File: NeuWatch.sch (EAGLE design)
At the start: 60 parts, among them IC1 SAMD21G18A-AUT, IC3 TPS2115, IC4 SIP32401A, IC5 MC74VHC1G14DFT, T1 846, T2 2N7002_ALT, Y1 32,768Khz

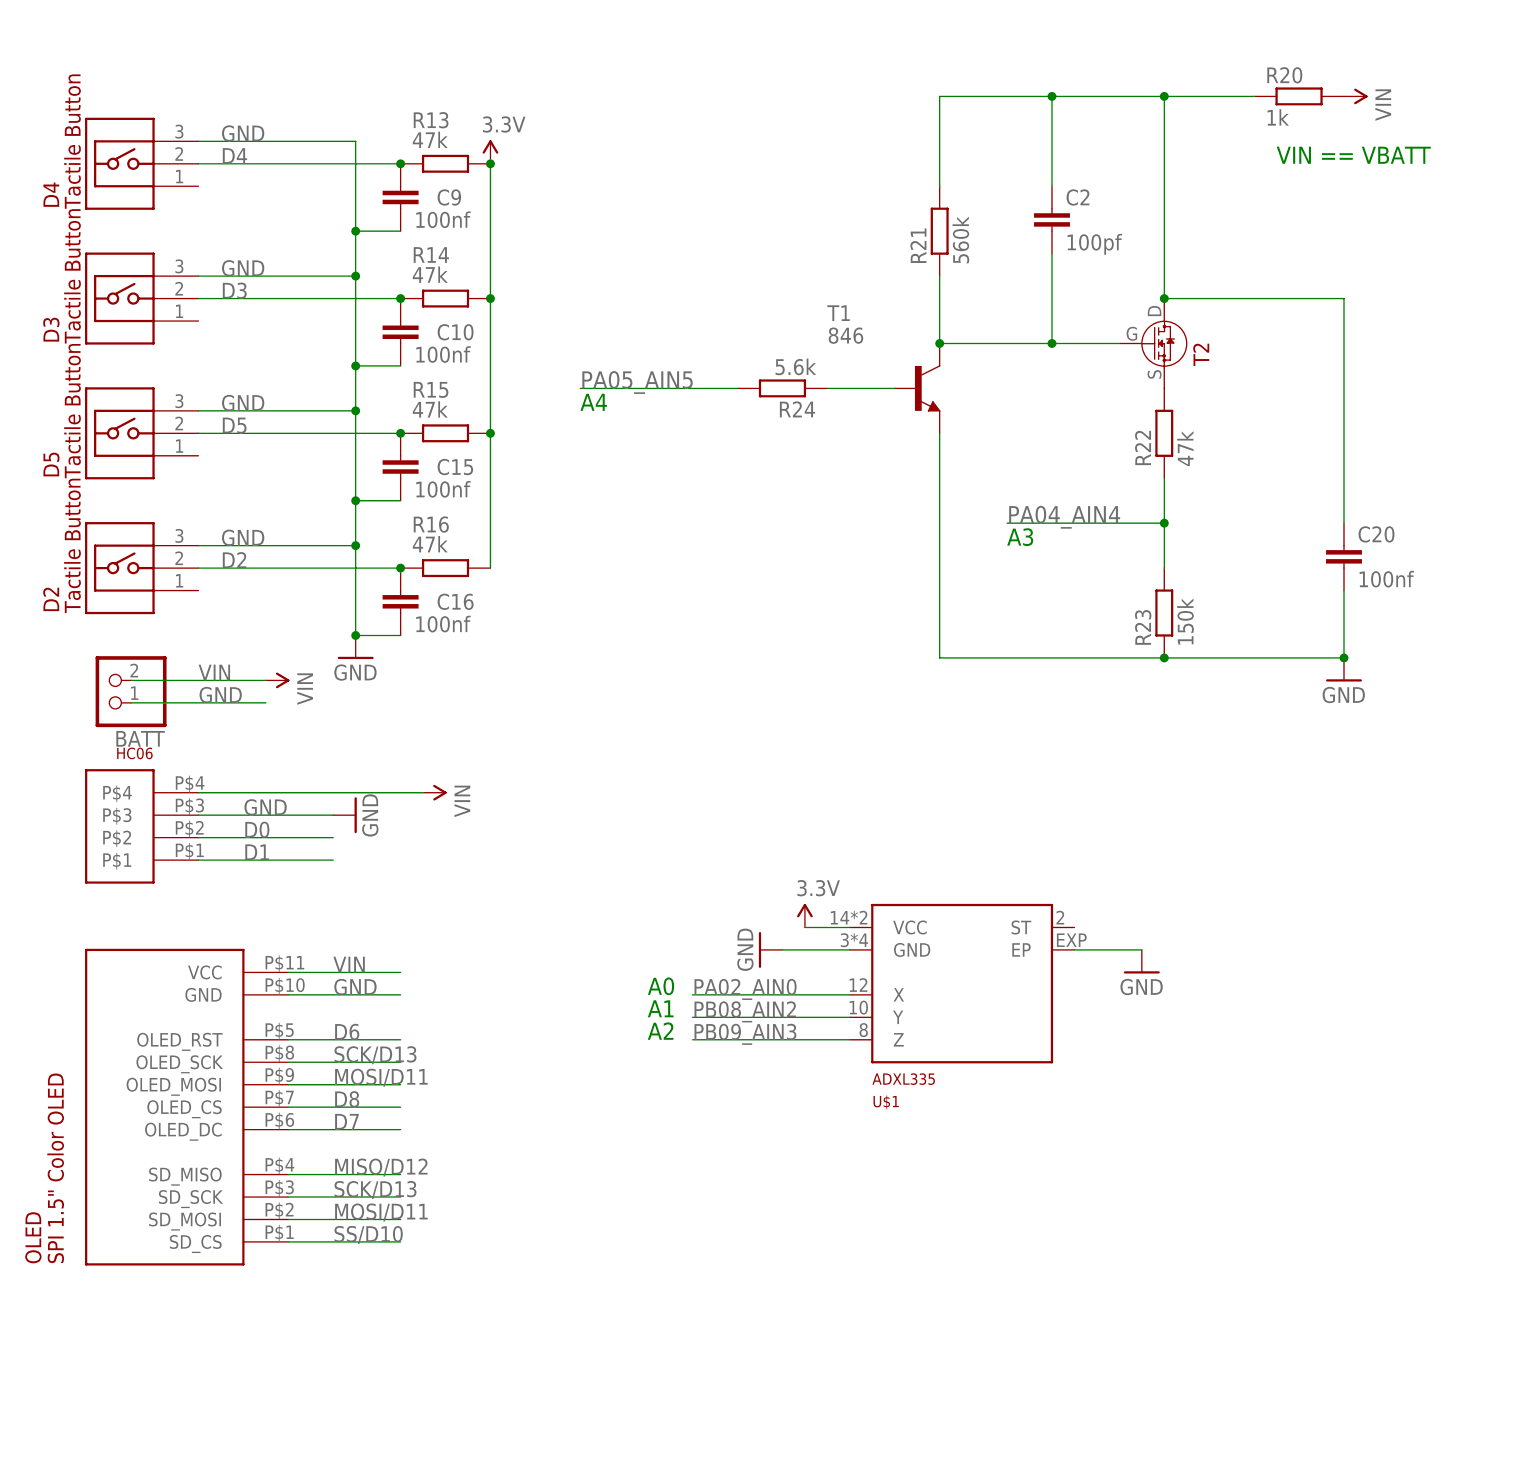
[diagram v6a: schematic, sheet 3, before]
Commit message: high side load
for OLED and UART cutoff
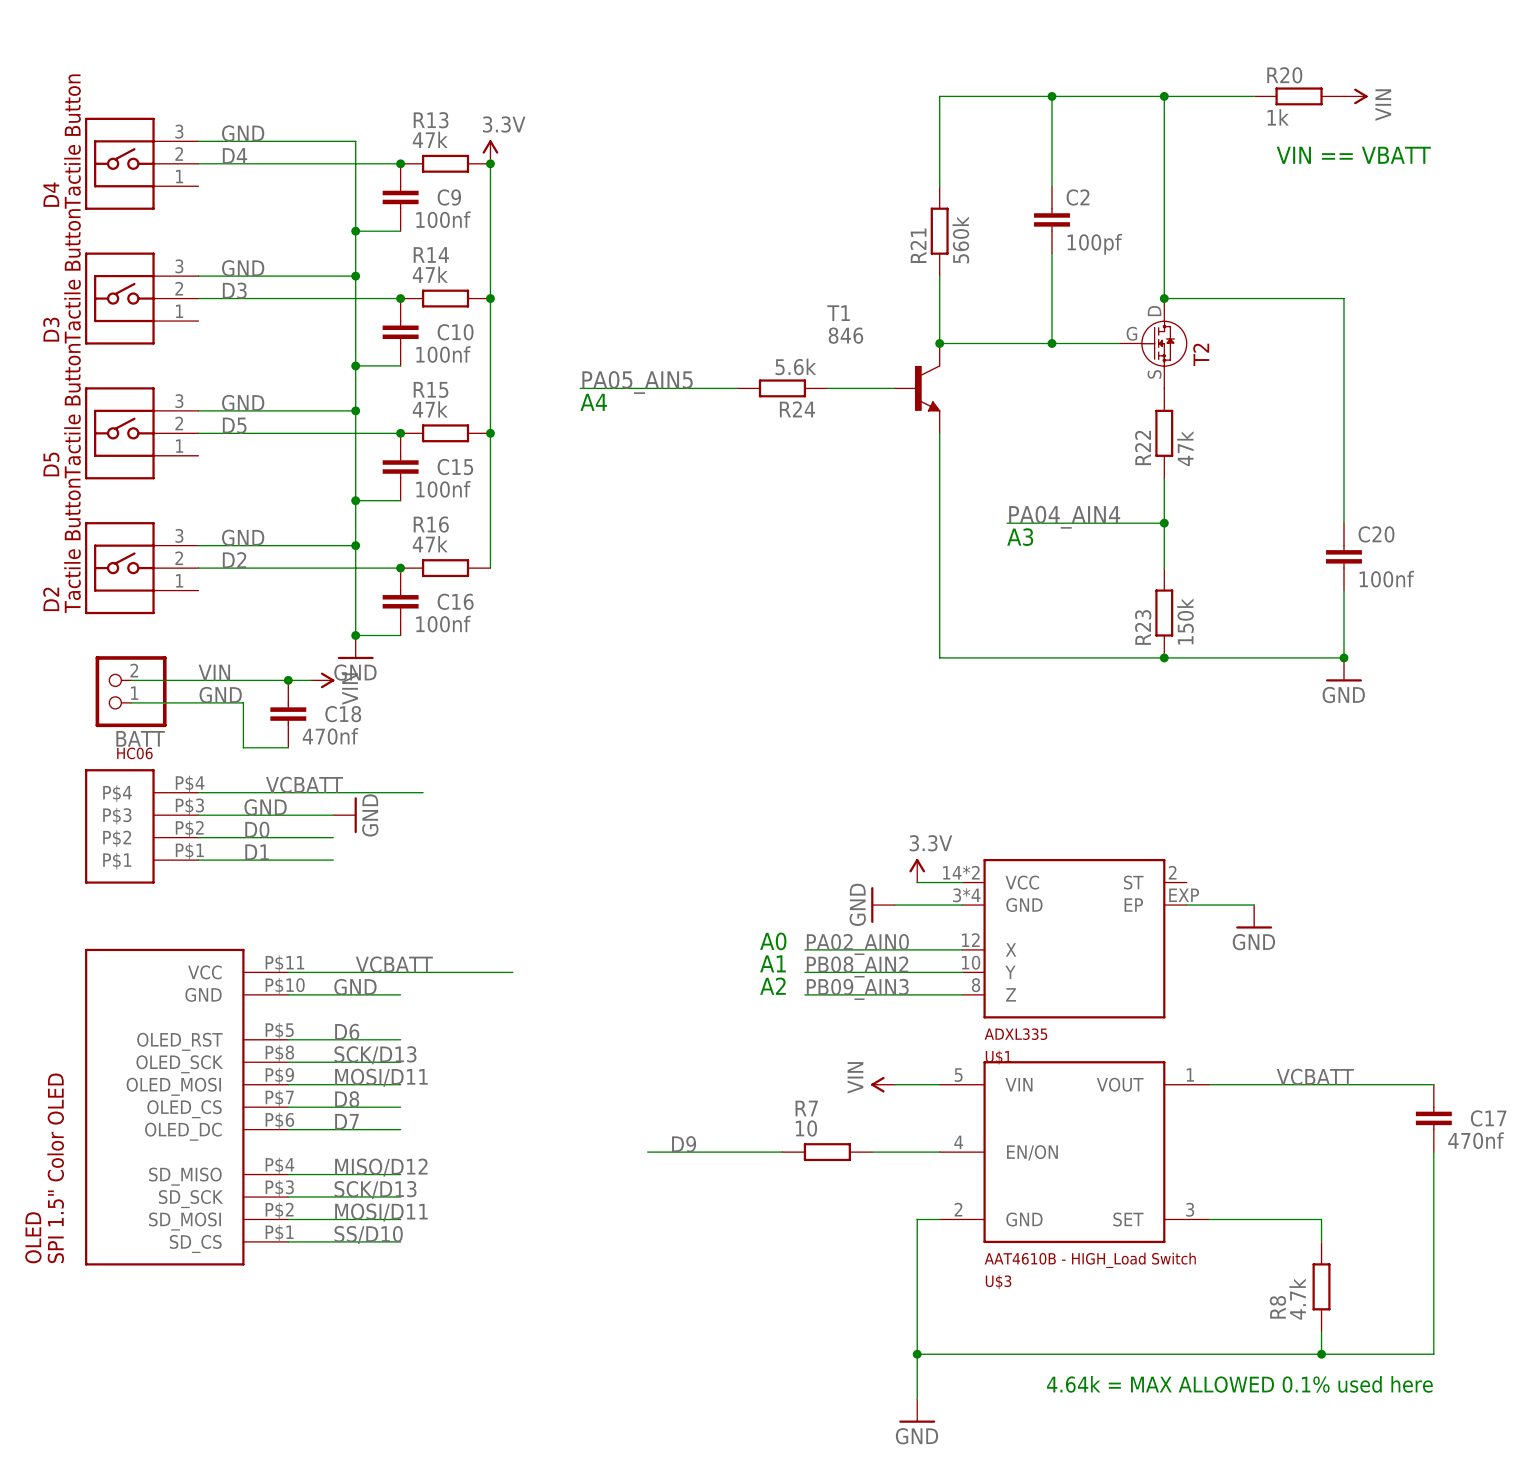
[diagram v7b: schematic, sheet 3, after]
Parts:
- added C17, C18: 470nf, AtomTech:CAPACITORC0402
- added R7: 10, rcl:R-EU_R0402
- added R8: 4.7k, rcl:R-EU_R0402
- added U$3: AAT4610B, AtomTech:AAT4610B
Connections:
- new net N$10: R7.2, U$3.EN/ON
- new net N$11: R8.2, U$3.SET
- new net VCBATT: C17.1, HC06.P$4, OLED.VCC, U$3.VOUT
- net D9: now also R7.1
- net GND: now also C17.2, C18.2, R8.1, U$3.GND
- net VIN: now also C18.1, U$3.VIN; no longer HC06.P$4, OLED.VCC
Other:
- note added: "4.64k = MAX ALLOWED 0.1% used here"
- moved on the sheet: U$1
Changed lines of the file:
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@@
 <part name="SUPPLY3" library="SparkFun-Aesthetics" deviceset="VIN" device=""/>
 <part name="GND1" library="supply1" deviceset="GND" device=""/>
+<part name="OLED" library="AtomTech" deviceset="1.5-OLED" device=""/>
+<part name="U$3" library="AtomTech" deviceset="AAT4610B" device=""/>
 <part name="SUPPLY4" library="SparkFun-Aesthetics" deviceset="VIN" device=""/>
-<part name="OLED" library="AtomTech" deviceset="1.5-OLED" device=""/>
+<part name="GND2" library="supply1" deviceset="GND" device=""/>
+<part name="R7" library="rcl" deviceset="R-EU_" device="R0402" value="10"/>
+<part name="R8" library="rcl" deviceset="R-EU_" device="R0402" value="4.7k"/>
+<part name="C17" library="AtomTech" deviceset="CAPACITOR" device="C0402" value="470nf"/>
+<part name="C18" library="AtomTech" deviceset="CAPACITOR" device="C0402" value="470nf"/>
 </parts>
 <sheets>
@@
 <text x="121.92" y="114.3" size="1.9304" layer="91">A3</text>
 <text x="152.4" y="157.48" size="1.9304" layer="91">VIN == VBATT</text>
-<text x="81.28" y="58.42" size="1.9304" layer="91">A2</text>
-<text x="81.28" y="60.96" size="1.9304" layer="91">A1</text>
-<text x="81.28" y="63.5" size="1.9304" layer="91">A0</text>
+<text x="93.98" y="63.5" size="1.9304" layer="91">A2</text>
+<text x="93.98" y="66.04" size="1.9304" layer="91">A1</text>
+<text x="93.98" y="68.58" size="1.9304" layer="91">A0</text>
+<text x="170.18" y="20.32" size="1.778" layer="91" rot="R180">4.64k = MAX ALLOWED 0.1% used here</text>
 </plain>
 <instances>
@@
 <instance part="HC06" gate="G$1" x="25.4" y="83.82" rot="R180"/>
 <instance part="BATT" gate="G$1" x="20.32" y="99.06" rot="R180"/>
-<instance part="SUPPLY16" gate="G$1" x="38.1" y="99.06" rot="R270"/>
+<instance part="SUPPLY16" gate="G$1" x="43.18" y="99.06" rot="R270"/>
 <instance part="GND5" gate="1" x="48.26" y="83.82" rot="R90"/>
 <instance part="GND19" gate="1" x="48.26" y="101.6"/>
@@
 <attribute name="VALUE" x="54.864" y="104.521" size="1.778" layer="96"/>
 </instance>
-<instance part="U$1" gate="G$1" x="116.84" y="63.5"/>
-<instance part="SUPPLY5" gate="G$1" x="99.06" y="71.12"/>
-<instance part="GND26" gate="1" x="93.98" y="68.58" rot="R270"/>
-<instance part="GND27" gate="1" x="137.16" y="66.04"/>
+<instance part="U$1" gate="G$1" x="129.54" y="68.58"/>
+<instance part="SUPPLY5" gate="G$1" x="111.76" y="76.2"/>
+<instance part="GND26" gate="1" x="106.68" y="73.66" rot="R270"/>
+<instance part="GND27" gate="1" x="149.86" y="71.12"/>
 <instance part="R20" gate="G$1" x="154.94" y="165.1"/>
 <instance part="R21" gate="G$1" x="114.3" y="149.86" rot="R90"/>
@@
 <instance part="SUPPLY3" gate="G$1" x="160.02" y="165.1" rot="R270"/>
 <instance part="GND1" gate="1" x="160.02" y="99.06"/>
-<instance part="SUPPLY4" gate="G$1" x="55.88" y="86.36" rot="R270"/>
 <instance part="OLED" gate="G$1" x="17.78" y="68.58"/>
+<instance part="U$3" gate="G$1" x="119.38" y="55.88"/>
+<instance part="SUPPLY4" gate="G$1" x="109.22" y="53.34" rot="R90"/>
+<instance part="GND2" gate="1" x="111.76" y="15.24"/>
+<instance part="R7" gate="G$1" x="101.6" y="45.72" smashed="yes">
+<attribute name="NAME" x="97.79" y="49.7586" size="1.778" layer="95"/>
+<attribute name="VALUE" x="97.79" y="47.498" size="1.778" layer="96"/>
+</instance>
+<instance part="R8" gate="G$1" x="157.48" y="30.48" smashed="yes" rot="R90">
+<attribute name="NAME" x="153.4414" y="26.67" size="1.778" layer="95" rot="R90"/>
+<attribute name="VALUE" x="155.702" y="26.67" size="1.778" layer="96" rot="R90"/>
+</instance>
+<instance part="C17" gate="G$1" x="170.18" y="50.8" smashed="yes">
+<attribute name="NAME" x="174.244" y="48.641" size="1.778" layer="95"/>
+<attribute name="VALUE" x="171.704" y="46.101" size="1.778" layer="96"/>
+</instance>
+<instance part="C18" gate="G$1" x="40.64" y="96.52" smashed="yes">
+<attribute name="NAME" x="44.704" y="94.361" size="1.778" layer="95"/>
+<attribute name="VALUE" x="42.164" y="91.821" size="1.778" layer="96"/>
+</instance>
 </instances>
 <busses>
@@
 <segment>
 <pinref part="BATT" gate="G$1" pin="1"/>
-<wire x1="22.86" y1="96.52" x2="38.1" y2="96.52" width="0.1524" layer="91"/>
+<wire x1="22.86" y1="96.52" x2="35.56" y2="96.52" width="0.1524" layer="91"/>
 <label x="30.48" y="96.52" size="1.778" layer="95"/>
+<pinref part="C18" gate="G$1" pin="2"/>
+<wire x1="40.64" y1="91.44" x2="35.56" y2="91.44" width="0.1524" layer="91"/>
+<wire x1="35.56" y1="91.44" x2="35.56" y2="96.52" width="0.1524" layer="91"/>
 </segment>
 <segment>
@@
 <pinref part="U$1" gate="G$1" pin="GND"/>
 <pinref part="GND26" gate="1" pin="GND"/>
-<wire x1="96.52" y1="68.58" x2="104.14" y2="68.58" width="0.1524" layer="91"/>
+<wire x1="109.22" y1="73.66" x2="116.84" y2="73.66" width="0.1524" layer="91"/>
 </segment>
 <segment>
 <pinref part="U$1" gate="G$1" pin="EP"/>
 <pinref part="GND27" gate="1" pin="GND"/>
-<wire x1="137.16" y1="68.58" x2="129.54" y2="68.58" width="0.1524" layer="91"/>
+<wire x1="149.86" y1="73.66" x2="142.24" y2="73.66" width="0.1524" layer="91"/>
 </segment>
 <segment>
@@
 <label x="45.72" y="63.5" size="1.778" layer="95"/>
 </segment>
+<segment>
+<pinref part="U$3" gate="G$1" pin="GND"/>
+<pinref part="GND2" gate="1" pin="GND"/>
+<wire x1="114.3" y1="38.1" x2="111.76" y2="38.1" width="0.1524" layer="91"/>
+<wire x1="111.76" y1="38.1" x2="111.76" y2="22.86" width="0.1524" layer="91"/>
+<pinref part="R8" gate="G$1" pin="1"/>
+<wire x1="111.76" y1="22.86" x2="111.76" y2="17.78" width="0.1524" layer="91"/>
+<wire x1="111.76" y1="22.86" x2="157.48" y2="22.86" width="0.1524" layer="91"/>
+<wire x1="157.48" y1="22.86" x2="157.48" y2="25.4" width="0.1524" layer="91"/>
+<junction x="111.76" y="22.86"/>
+<pinref part="C17" gate="G$1" pin="2"/>
+<wire x1="157.48" y1="22.86" x2="170.18" y2="22.86" width="0.1524" layer="91"/>
+<wire x1="170.18" y1="22.86" x2="170.18" y2="45.72" width="0.1524" layer="91"/>
+<junction x="157.48" y="22.86"/>
+</segment>
 </net>
 <net name="D6" class="0">
@@
 <segment>
 <pinref part="BATT" gate="G$1" pin="2"/>
-<wire x1="22.86" y1="99.06" x2="38.1" y2="99.06" width="0.1524" layer="91"/>
+<wire x1="22.86" y1="99.06" x2="40.64" y2="99.06" width="0.1524" layer="91"/>
 <label x="30.48" y="99.06" size="1.778" layer="95"/>
 <pinref part="SUPPLY16" gate="G$1" pin="VIN"/>
+<pinref part="C18" gate="G$1" pin="1"/>
+<wire x1="40.64" y1="99.06" x2="43.18" y2="99.06" width="0.1524" layer="91"/>
+<junction x="40.64" y="99.06"/>
 </segment>
 <segment>
@@
 </segment>
 <segment>
-<pinref part="HC06" gate="G$1" pin="P$4"/>
+<pinref part="U$3" gate="G$1" pin="VIN"/>
 <pinref part="SUPPLY4" gate="G$1" pin="VIN"/>
-<wire x1="55.88" y1="86.36" x2="30.48" y2="86.36" width="0.1524" layer="91"/>
-</segment>
-<segment>
-<wire x1="53.34" y1="66.04" x2="40.64" y2="66.04" width="0.1524" layer="91"/>
-<pinref part="OLED" gate="G$1" pin="VCC"/>
-<label x="45.72" y="66.04" size="1.778" layer="95"/>
+<wire x1="109.22" y1="53.34" x2="114.3" y2="53.34" width="0.1524" layer="91"/>
 </segment>
 </net>
@@
 <pinref part="U$1" gate="G$1" pin="VCC"/>
 <pinref part="SUPPLY5" gate="G$1" pin="3.3V"/>
-<wire x1="99.06" y1="71.12" x2="104.14" y2="71.12" width="0.1524" layer="91"/>
+<wire x1="111.76" y1="76.2" x2="116.84" y2="76.2" width="0.1524" layer="91"/>
 </segment>
 </net>
@@
 <segment>
 <pinref part="U$1" gate="G$1" pin="X"/>
-<wire x1="86.36" y1="63.5" x2="104.14" y2="63.5" width="0.1524" layer="91"/>
-<label x="86.36" y="63.5" size="1.778" layer="95"/>
+<wire x1="99.06" y1="68.58" x2="116.84" y2="68.58" width="0.1524" layer="91"/>
+<label x="99.06" y="68.58" size="1.778" layer="95"/>
 </segment>
 </net>
@@
 <segment>
 <pinref part="U$1" gate="G$1" pin="Y"/>
-<wire x1="86.36" y1="60.96" x2="104.14" y2="60.96" width="0.1524" layer="91"/>
-<label x="86.36" y="60.96" size="1.778" layer="95"/>
+<wire x1="99.06" y1="66.04" x2="116.84" y2="66.04" width="0.1524" layer="91"/>
+<label x="99.06" y="66.04" size="1.778" layer="95"/>
 </segment>
 </net>
@@
 <segment>
 <pinref part="U$1" gate="G$1" pin="Z"/>
-<wire x1="86.36" y1="58.42" x2="104.14" y2="58.42" width="0.1524" layer="91"/>
-<label x="86.36" y="58.42" size="1.778" layer="95"/>
+<wire x1="99.06" y1="63.5" x2="116.84" y2="63.5" width="0.1524" layer="91"/>
+<label x="99.06" y="63.5" size="1.778" layer="95"/>
 </segment>
 </net>
@@
 </segment>
 </net>
+<net name="N$10" class="0">
+<segment>
+<pinref part="U$3" gate="G$1" pin="EN/ON"/>
+<wire x1="114.3" y1="45.72" x2="106.68" y2="45.72" width="0.1524" layer="91"/>
+<pinref part="R7" gate="G$1" pin="2"/>
+</segment>
+</net>
+<net name="D9" class="0">
+<segment>
+<pinref part="R7" gate="G$1" pin="1"/>
+<wire x1="96.52" y1="45.72" x2="81.28" y2="45.72" width="0.1524" layer="91"/>
+<label x="83.82" y="45.72" size="1.778" layer="95"/>
+</segment>
+</net>
+<net name="N$11" class="0">
+<segment>
+<pinref part="U$3" gate="G$1" pin="SET"/>
+<pinref part="R8" gate="G$1" pin="2"/>
+<wire x1="144.78" y1="38.1" x2="157.48" y2="38.1" width="0.1524" layer="91"/>
+<wire x1="157.48" y1="38.1" x2="157.48" y2="35.56" width="0.1524" layer="91"/>
+</segment>
+</net>
+<net name="VCBATT" class="0">
+<segment>
+<pinref part="U$3" gate="G$1" pin="VOUT"/>
+<wire x1="144.78" y1="53.34" x2="170.18" y2="53.34" width="0.1524" layer="91"/>
+<label x="152.4" y="53.34" size="1.778" layer="95"/>
+<pinref part="C17" gate="G$1" pin="1"/>
+</segment>
+<segment>
+<wire x1="40.64" y1="66.04" x2="66.04" y2="66.04" width="0.1524" layer="91"/>
+<label x="48.26" y="66.04" size="1.778" layer="95"/>
+<pinref part="OLED" gate="G$1" pin="VCC"/>
+</segment>
+<segment>
+<wire x1="30.48" y1="86.36" x2="55.88" y2="86.36" width="0.1524" layer="91"/>
+<label x="38.1" y="86.36" size="1.778" layer="95"/>
+<pinref part="HC06" gate="G$1" pin="P$4"/>
+</segment>
+</net>

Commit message: fixes
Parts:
- L1: value 1.5 uH -> 120 nH
- RESET: device parts:TACTILE_SWITCH -> AtomTech:TACTILE_SWITCH
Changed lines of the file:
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@@
 <part name="U$2" library="AtomTech" deviceset="USB_GENERIC" device="_CHEAT"/>
 <part name="SUPPLY16" library="SparkFun-Aesthetics" deviceset="VIN" device=""/>
-<part name="RESET" library="parts" deviceset="TACTILE_SWITCH" device=""/>
+<part name="RESET" library="AtomTech" deviceset="TACTILE_SWITCH" device=""/>
 <part name="MCP" library="parts" deviceset="MCP73831" device=""/>
 <part name="C12" library="AtomTech" deviceset="CAPACITOR" device="C0402" value="4.7uF"/>
@@
 <part name="GND22" library="supply1" deviceset="GND" device=""/>
 <part name="GND23" library="supply1" deviceset="GND" device=""/>
-<part name="L1" library="Bourns_By_element14_Batch_1" deviceset="PM0603-R12J-RC" device="" value="1.5 uH"/>
+<part name="L1" library="Bourns_By_element14_Batch_1" deviceset="PM0603-R12J-RC" device="" value="120 nH"/>
 <part name="C14" library="AtomTech" deviceset="CAPACITOR" device="C0402" value="10 uF"/>
 <part name="GND24" library="supply1" deviceset="GND" device=""/>
